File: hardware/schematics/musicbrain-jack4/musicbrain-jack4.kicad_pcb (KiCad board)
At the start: 2 copper layers, 20 x 65 mm, 6 parts, among them J1 SOCKET-BACK, J2 PJ398SM, J3 PJ398SM, J4 PJ398SM, J5 PJ398SM

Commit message: jack8/jack4 v1.2 + pot8front v1.1: koppel-standaard + 3D-socket-fix
- Front-koppeling gestandaardiseerd: 1x10-socket op x=116,5 (16,5 van west-
  rand), pin 1 op y=143,57 - identiek op jack8, jack4 en pot8front
- B-zijde-sockets nu in KiCads canonieke geflipte vorm (rot 180, lokale y
  genegeerd): koper ongewijzigd, maar het 3D-model staat nu OP de gatenrij
  i.p.v. ernaast gespiegeld
- PCB-papier naar A3 (borden vielen van A4-landscape af), silk-URL naar
  bordmidden (viel over de bordrand door center-justify)
- make_fab.sh: bordenlijst actueel (deprecated eruit, fronts erin),
  selectie-argument + gerber-zip-stap toegevoegd
- ERC/netcheck/DRC 0/0 op alle drie; fab + PDF's ververst

Co-Authored-By: Claude Fable 5 <noreply@anthropic.com>
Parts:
- moved J1 17.5 mm to (116.5, 143.6), turned to 180 degrees
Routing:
- net /CH2: track 20.1 -> 39.1 mm
- net /CH1: track 32.6 -> 51.5 mm
- net /CH3: track 7.69 -> 26.6 mm
- net /CH4: track 18.8 -> 14.1 mm
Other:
- board text added: "musicbrain.nl/hw/jack4 rev 1.2"
- board text removed: "musicbrain.nl/hw/jack4 rev 1.1"
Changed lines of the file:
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@@
   (generator_version "8.0")
   (general (thickness 1.6) (legacy_teardrops no))
-  (paper "A4")
+  (paper "A3")
   (title_block
     (title "MusicBrain jack4")
-    (date "2026-07-08")
-    (rev "1.1")
+    (date "2026-07-11")
+    (rev "1.2")
     (company "MusicBrain project")
   )
@@
   (footprint "MusicBrain:Header_1x06_backside"
     (layer "B.Cu")
-    (at 115 126.15)
+    (at 116.5 143.57 180)
     (descr "1x6 female socket op de ACHTERZIJDE (opening omlaag, naar de kaart)")
-    (property "Reference" "J1" (at 2.8 -2.2 0) (layer "B.SilkS")
+    (property "Reference" "J1" (at -2.8 2.2 0) (layer "B.SilkS")
       (effects (font (size 1 1) (thickness 0.15)) (justify mirror)))
-    (property "Value" "SOCKET-BACK" (at 0 15.7 0) (layer "B.Fab")
+    (property "Value" "SOCKET-BACK" (at 0 -15.7 0) (layer "B.Fab")
       (effects (font (size 1 1) (thickness 0.15)) (justify mirror)))
     (attr through_hole)
-    (fp_rect (start -1.6 -1.6) (end 1.6 14.3)
+    (fp_rect (start -1.6 -14.3) (end 1.6 1.6)
       (stroke (width 0.12) (type solid)) (fill no) (layer "B.SilkS"))
-    (fp_rect (start -1.8 -1.8) (end 1.8 14.5)
+    (fp_rect (start -1.8 -14.5) (end 1.8 1.8)
       (stroke (width 0.05) (type solid)) (fill no) (layer "B.CrtYd"))
-    (pad "1" thru_hole rect (at 0 0) (size 1.7 1.7) (drill 1.0) (layers "*.Cu" "*.Mask") (net 1 "GND"))
-    (pad "2" thru_hole oval (at 0 2.54) (size 1.7 1.7) (drill 1.0) (layers "*.Cu" "*.Mask") (net 3 "/CH1"))
-    (pad "3" thru_hole oval (at 0 5.08) (size 1.7 1.7) (drill 1.0) (layers "*.Cu" "*.Mask") (net 4 "/CH2"))
-    (pad "4" thru_hole oval (at 0 7.62) (size 1.7 1.7) (drill 1.0) (layers "*.Cu" "*.Mask") (net 5 "/CH3"))
-    (pad "5" thru_hole oval (at 0 10.16) (size 1.7 1.7) (drill 1.0) (layers "*.Cu" "*.Mask") (net 6 "/CH4"))
-    (pad "6" thru_hole oval (at 0 12.7) (size 1.7 1.7) (drill 1.0) (layers "*.Cu" "*.Mask") (net 1 "GND"))
+    (pad "1" thru_hole rect (at 0 -0 180) (size 1.7 1.7) (drill 1.0) (layers "*.Cu" "*.Mask") (net 1 "GND"))
+    (pad "2" thru_hole oval (at 0 -2.54 180) (size 1.7 1.7) (drill 1.0) (layers "*.Cu" "*.Mask") (net 3 "/CH1"))
+    (pad "3" thru_hole oval (at 0 -5.08 180) (size 1.7 1.7) (drill 1.0) (layers "*.Cu" "*.Mask") (net 4 "/CH2"))
+    (pad "4" thru_hole oval (at 0 -7.62 180) (size 1.7 1.7) (drill 1.0) (layers "*.Cu" "*.Mask") (net 5 "/CH3"))
+    (pad "5" thru_hole oval (at 0 -10.16 180) (size 1.7 1.7) (drill 1.0) (layers "*.Cu" "*.Mask") (net 6 "/CH4"))
+    (pad "6" thru_hole oval (at 0 -12.7 180) (size 1.7 1.7) (drill 1.0) (layers "*.Cu" "*.Mask") (net 1 "GND"))
     (model "${KICAD10_3DMODEL_DIR}/Connector_PinSocket_2.54mm.3dshapes/PinSocket_1x06_P2.54mm_Vertical.step"
       (offset (xyz 0 0 0)) (scale (xyz 1 1 1)) (rotate (xyz 0 0 0)))
@@
       (net 1 "GND"))
   )
-  (segment (start 115 128.69) (end 111.05 128.69) (width 0.25) (layer "F.Cu") (net 3))
-  (segment (start 111.05 128.69) (end 111.05 103.08) (width 0.25) (layer "F.Cu") (net 3))
-  (segment (start 111.05 103.08) (end 108 103.08) (width 0.25) (layer "F.Cu") (net 3))
-  (segment (start 115 131.23) (end 110.55 131.23) (width 0.25) (layer "F.Cu") (net 4))
-  (segment (start 110.55 131.23) (end 110.55 118.08) (width 0.25) (layer "F.Cu") (net 4))
-  (segment (start 110.55 118.08) (end 108 118.08) (width 0.25) (layer "F.Cu") (net 4))
-  (segment (start 115 133.77) (end 110.05 133.77) (width 0.25) (layer "F.Cu") (net 5))
-  (segment (start 110.05 133.77) (end 110.05 133.08) (width 0.25) (layer "F.Cu") (net 5))
-  (segment (start 110.05 133.08) (end 108 133.08) (width 0.25) (layer "F.Cu") (net 5))
-  (segment (start 115 136.31) (end 111.55 136.31) (width 0.25) (layer "F.Cu") (net 6))
-  (segment (start 111.55 136.31) (end 111.55 148.08) (width 0.25) (layer "F.Cu") (net 6))
-  (segment (start 111.55 148.08) (end 108 148.08) (width 0.25) (layer "F.Cu") (net 6))
+  (segment (start 116.5 146.11) (end 111.55 146.11) (width 0.25) (layer "F.Cu") (net 3))
+  (segment (start 111.55 146.11) (end 111.55 103.08) (width 0.25) (layer "F.Cu") (net 3))
+  (segment (start 111.55 103.08) (end 108 103.08) (width 0.25) (layer "F.Cu") (net 3))
+  (segment (start 116.5 148.65) (end 111.05 148.65) (width 0.25) (layer "F.Cu") (net 4))
+  (segment (start 111.05 148.65) (end 111.05 118.08) (width 0.25) (layer "F.Cu") (net 4))
+  (segment (start 111.05 118.08) (end 108 118.08) (width 0.25) (layer "F.Cu") (net 4))
+  (segment (start 116.5 151.19) (end 110.55 151.19) (width 0.25) (layer "F.Cu") (net 5))
+  (segment (start 110.55 151.19) (end 110.55 133.08) (width 0.25) (layer "F.Cu") (net 5))
+  (segment (start 110.55 133.08) (end 108 133.08) (width 0.25) (layer "F.Cu") (net 5))
+  (segment (start 116.5 153.73) (end 110.05 153.73) (width 0.25) (layer "F.Cu") (net 6))
+  (segment (start 110.05 153.73) (end 110.05 148.08) (width 0.25) (layer "F.Cu") (net 6))
+  (segment (start 110.05 148.08) (end 108 148.08) (width 0.25) (layer "F.Cu") (net 6))
   (segment (start 108 111.38) (end 103.5 111.38) (width 0.3) (layer "F.Cu") (net 2))
   (segment (start 103.5 111.38) (end 103.5 159) (width 0.3) (layer "F.Cu") (net 2))
@@
     (stroke (width 0.1) (type default)) (fill none)
     (layer "Edge.Cuts"))
-  (gr_text "musicbrain.nl/hw/jack4 rev 1.1" (at 101.3 163 90) (layer "F.SilkS")
+  (gr_text "musicbrain.nl/hw/jack4 rev 1.2" (at 101.3 132.5 90) (layer "F.SilkS")
     (effects (font (size 1 1) (thickness 0.15))))
   (zone (net 1) (net_name "GND") (layer "F.Cu")

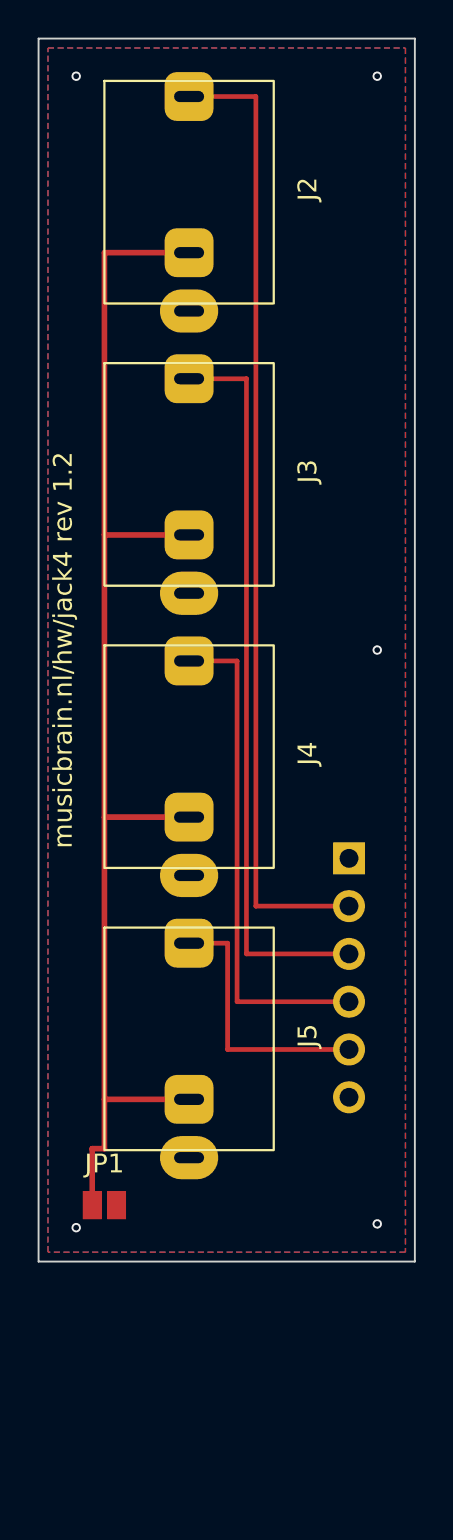
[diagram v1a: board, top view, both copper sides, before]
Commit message: jack8/jack4 gen 2: steek 13,75; jack8 110 mm met socket op het hart
- jacksteek 15 -> 13,75 (4 HP-front, = pot8front); jack8 125 -> 110 mm
  (past nu tussen de rails); socket op HY0 143,57 = exact gecentreerd
- jack4 alleen de steek (kabelbord aan de hub-DAC, centrering irrelevant)
- Thonkiconn-pads in y geslankt (tip 1,8 / sleeve 1,5; annular >= 0,45,
  slot 1,6x0,6) - op 13,75 raakten de gen-1-pads elkaar; courtyard strak
  om body+pads (was 15-steek-maat)
- jackkolom op de pad-envelop gecentreerd (envelop is 0,7 asymmetrisch);
  rand-marge expliciet 0,3 (JLC-minimum) in de .kicad_pro
- JP1 naar BY1-1,5 + NORM-rail doorgetrokken; hechtvia uit de JP1-zone
- beide: ERC 0, netcheck OK, DRC 0/0

Co-Authored-By: Claude Fable 5 <noreply@anthropic.com>
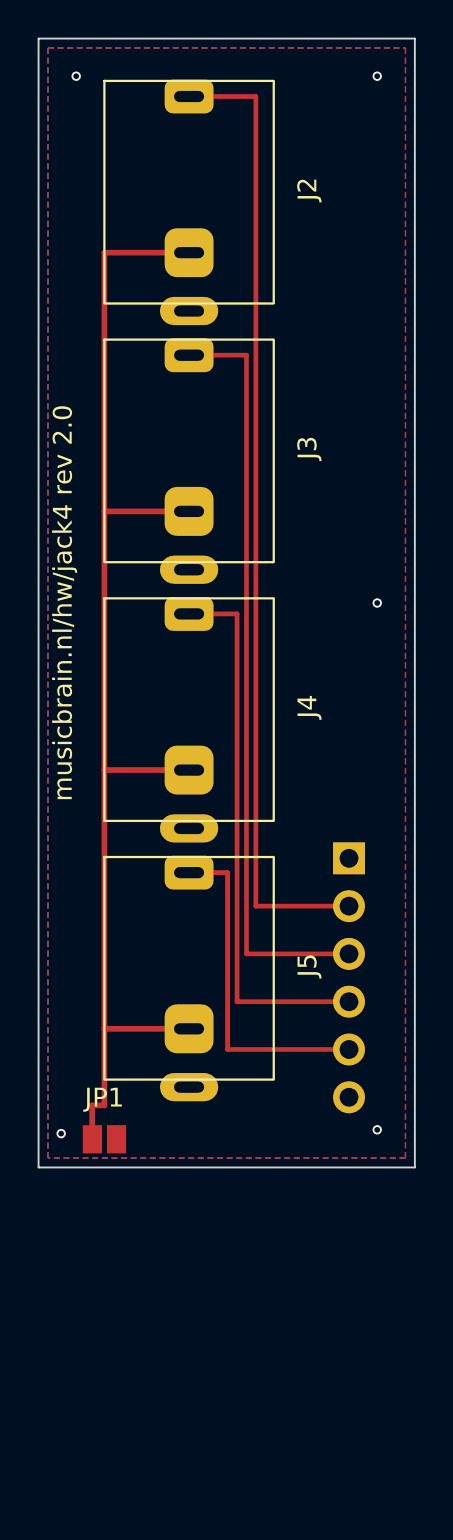
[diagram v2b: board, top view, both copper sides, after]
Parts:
- moved J5 3.75 mm to (108.0, 149.2)
- moved JP1 3.50 mm to (103.5, 158.5)
- moved J4 2.50 mm to (108.0, 135.5)
- moved J3 1.25 mm to (108.0, 121.8)
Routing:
- net /CH4: track 14.1 -> 17.9 mm
- net /NORM: track 69.3 -> 65.8 mm
- net /CH3: track 26.6 -> 29.1 mm
- net /CH2: track 39.1 -> 40.3 mm
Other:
- board size 20 x 65 mm -> 20 x 60 mm
- board text added: "musicbrain.nl/hw/jack4 rev 2.0"
- board text removed: "musicbrain.nl/hw/jack4 rev 1.2"
